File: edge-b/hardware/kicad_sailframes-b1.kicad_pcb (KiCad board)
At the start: 2 copper layers, 79.5 x 89.3 mm, 76 parts, among them J10 I2C_EXP1, J11 I2C_EXP2, J12 I2C_EXP3, J13 GPIO_EXP, J14 UART_DBG, J15 J_AUX, J16 GNSS_DBG, J17 LATCH_DBG, J2 JST_PH_BAT, J3 U.FL, J5 MICROSD, J8 BNO085_SOCKET, J9 HOSYOND_3.5_TFT, U1 LC29HEAMD, U2 TP4056, U3 MT3608, U4 ESP32_DEVKIT_V1

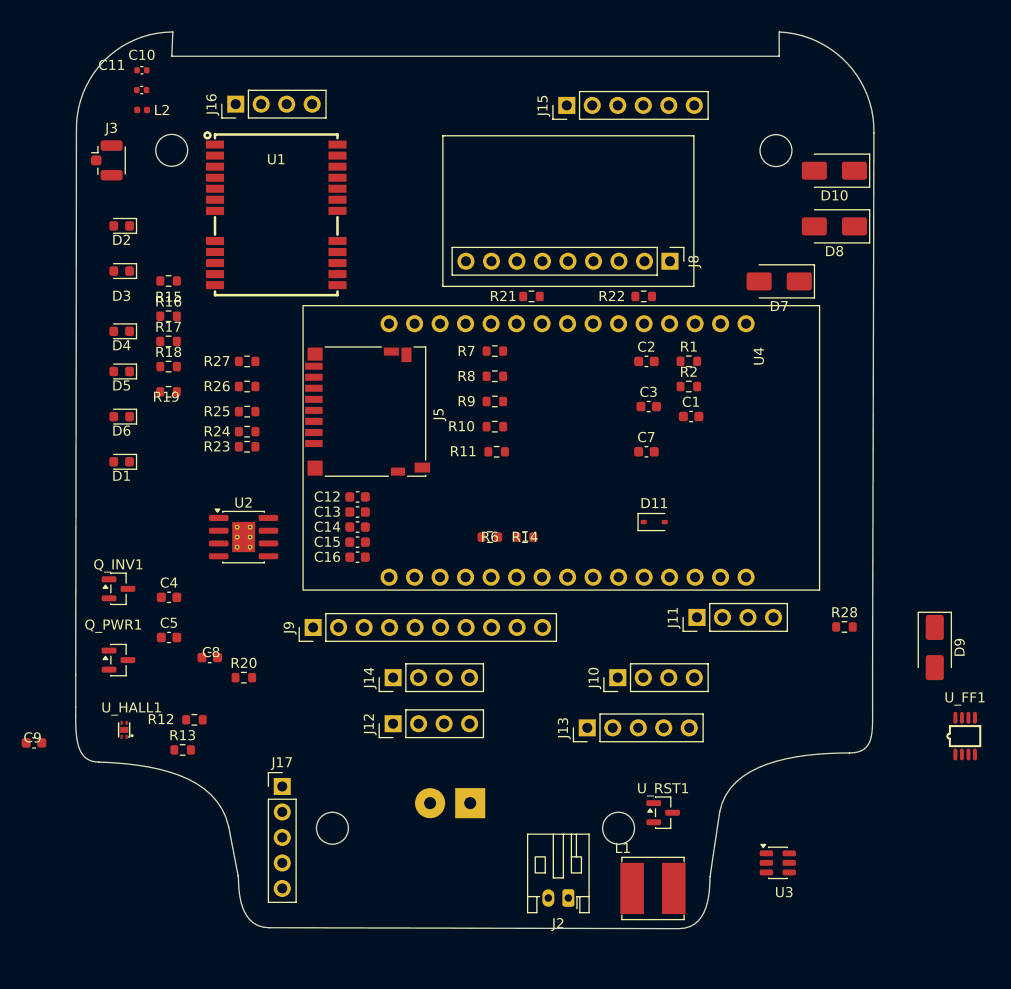
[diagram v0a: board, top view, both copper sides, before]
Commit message: B1 PCB: route board + DRC-clean, fix power/IMU bugs, add fab outputs
- Boost: fix inductor topology (L1 was out of the power path)
- D7 reversed to Option A (TP4056_VCC -> V5_SW); add C17 V_BCKP bypass
- J8 -> 10-pin GY-BNO08X pinout (3V3/GND/SCL/SDA), addr 0x4B
- Switcher re-placed tight; 4 mounting-hole keepouts (5.7mm)
- LED function silk (QI/CHRG/DONE/HB/GPS/SD); D/R refs moved to F.Fab
- Net classes (Power 0.5mm); fully routed, 0 DRC violations
- JLC fab package: gerbers, drill, BOM (bom-jlcpcb.csv), CPL

Co-Authored-By: Claude Opus 4.8 (1M context) <noreply@anthropic.com>
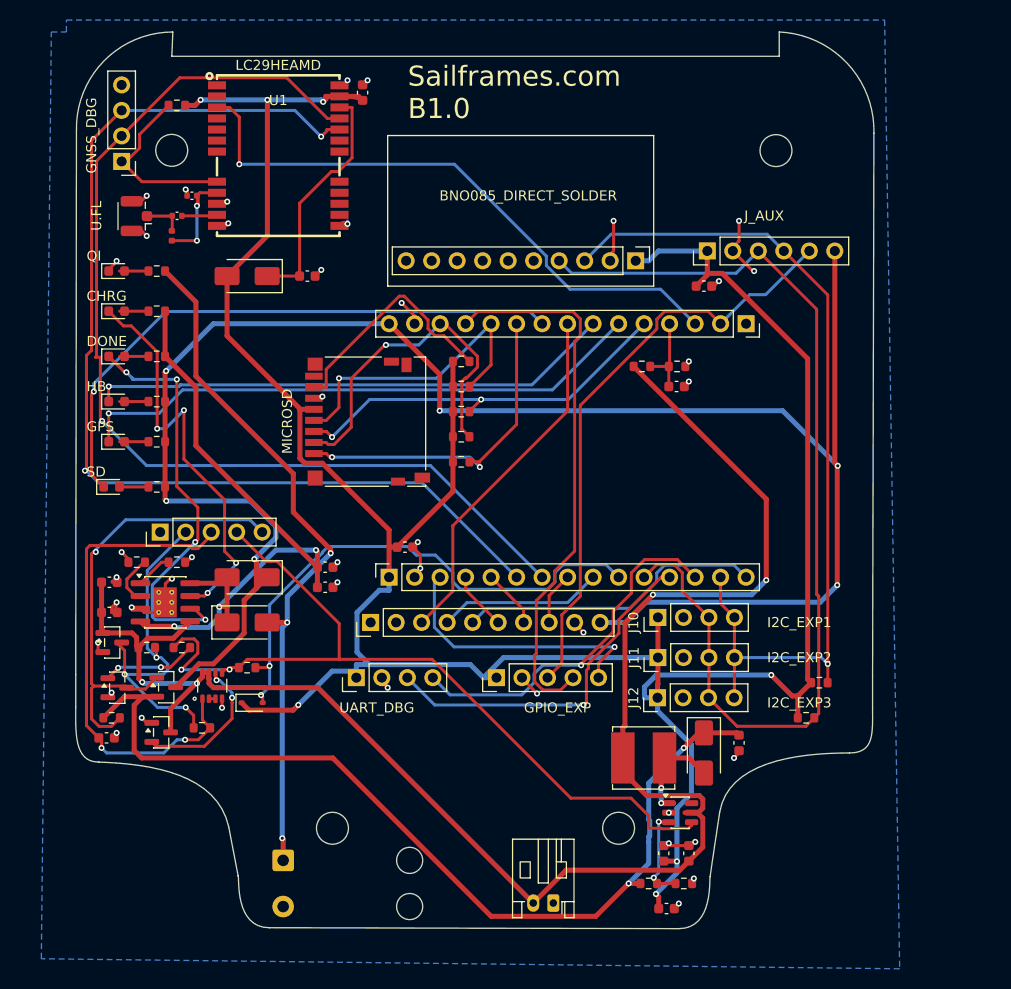
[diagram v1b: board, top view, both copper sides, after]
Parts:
- removed U4: ESP32_DEVKIT_V1, b1_Library:ESP32DEVIKITV1
- added C17: 100nF, Capacitor_SMD:C_0603_1608Metric, F.Cu at (123.0, 89.5)
- added J1: Conn_01x15, Connector_PinSocket_2.54mm:PinSocket_1x15_P2.54mm_Vertical, F.Cu at (166.7, 94.2)
- added J4: Conn_01x15, Connector_PinSocket_2.54mm:PinSocket_1x15_P2.54mm_Vertical, F.Cu at (131.1, 119.5)
- J8: value BNO085_SOCKET -> BNO085_DIRECT_SOLDER; footprint Connector_PinHeader_2.54mm:PinHeader_1x09_P2.54mm_Vertical -> Connector_PinHeader_2.54mm:PinHeader_1x10_P2.54mm_Vertical
- J_QI1: footprint Connector_PinHeader_2.54mm:PinHeader_1x02_P2.54mm_Vertical -> Connector_Wire:SolderWire-0.5sqmm_1x02_P4.6mm_D0.9mm_OD2.1mm_Relief
- R17, R18, R19: value 220 -> 1k
- U_FF1: footprint B1_JLC:SM8_L3.0-W2.8-P0.65-LS4.0-BL -> B1_JLC:VSSOP-8_DCU_2.3x2mm_P0.65mm
- U_HALL1: value DRV5032AJ -> DRV5032AJDBZR; footprint B1_DRV5032AJ:X2SON-4_L1.1-W1.4-P0.50-BR-EP -> Package_TO_SOT_SMD:SOT-23
- moved U_FF1 75.2 mm to (113.5, 130.3)
- moved D8 70.6 mm to (117.0, 124.0), turned to 0 degrees
- moved D7 60.6 mm to (117.0, 119.5)
- moved R28 59.6 mm to (117.0, 128.5)
- moved D10 59.4 mm to (117.0, 89.5)
- moved C8 53.4 mm to (166.0, 136.0), turned to -90 degrees
- moved U_RST1 50.6 mm to (108.4, 134.9)
- moved R21 50.1 mm to (172.7, 133.5)
- moved C13 50.1 mm to (158.8, 152.5)
- moved R10 48.0 mm to (157.0, 150.0)
- moved R11 46.9 mm to (160.5, 150.0)
- moved C12 46.8 mm to (158.5, 147.0), turned to 90 degrees
- moved C15 44.8 mm to (128.5, 71.2), turned to 90 degrees
- moved D11 43.9 mm to (117.5, 132.0)
- moved R15 43.9 mm to (103.5, 133.5)
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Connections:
- D2 pad 1: /D2_ANODE -> /TP_CHRG
- D7 pad 1: /TP4056_VCC -> /V5_SW
- D7 pad 2: /V5_SW -> /TP4056_VCC
- D9 pad 2: /BOOST_OUT -> /MT3608_SW
- J8 pad 2: unconnected-(J8-Pin_2-Pad2) -> /GND
- J8 pad 3: /GND -> /I2C_SCL
- J8 pad 5: /I2C_SCL -> unconnected-(J8-Pin_5-Pad5)
- L1 pad 1: /MT3608_SW -> /VBAT
- L1 pad 2: /BOOST_OUT -> /MT3608_SW
- R8 pad 2: /V5_SW -> /TP4056_VCC
- R9 pad 2: /V5_SW -> /TP4056_VCC
- U2 pad 7: /D2_ANODE -> /TP_CHRG
- U_HALL1 pad 3: unconnected-(U_HALL1-NC-Pad3) -> /HALL_OUT
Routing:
- net /V3V3: track 0.00 -> 270.7 mm, vias 0 -> 7
- net /V5_SW: track 0.00 -> 183.1 mm, vias 0 -> 6
- net /VBAT: track 0.00 -> 170.4 mm, vias 0 -> 4
- net /GNSS_TXD: track 0.00 -> 108.0 mm, vias 0 -> 2
- net /GNSS_RXD: track 0.00 -> 106.1 mm, vias 0 -> 1
- net /I2C_SDA: track 0.00 -> 101.0 mm
- net /V5_UNSW: track 0.00 -> 94.0 mm, vias 0 -> 2
- net /I2C_SCL: track 0.00 -> 88.6 mm, vias 0 -> 1
- net /LATCH_Q: track 0.00 -> 84.1 mm, vias 0 -> 2
- net /V_QI: track 0.00 -> 69.6 mm, vias 0 -> 3
- net /TP4056_VCC: track 0.00 -> 66.0 mm, vias 0 -> 3
- net /GND: track 0.00 -> 62.2 mm, vias 0 -> 42
- net /GNSS_1PPS: track 0.00 -> 59.8 mm, vias 0 -> 1
- net /LED_SD_N: track 0.00 -> 59.4 mm, vias 0 -> 1
- net /AUX_INT: track 0.00 -> 59.2 mm
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- added copper zone on B.Cu, net /GND
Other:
- board text added: "+"
- board text added: "CHRG"
- board text added: "DONE"
- board text added: "GND"
- board text added: "GPS"
- board text added: "HB"
- board text added: "QI"
- board text added: "SD"
- board text added: "Sailframes.com B1.0"
